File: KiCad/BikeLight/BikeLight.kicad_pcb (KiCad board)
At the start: 2 copper layers, 17 parts, among them J1 Conn-01x02_P2.5mm_S2B-XH-A-BK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, J3 Conn-01x02_P2.5mm_S2B-XH-A-BK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, SW1 CK_KMS2xxG, U1 HT-CT62, U2 MPU-6050, U3 MCP1826S-33, U4 MAX17048, U5 TP4056-42-ESOP8

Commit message: Added power protection, annotated
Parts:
- added C8: 100n_0603_TCC0603X7R104K500CT, Capacitor_SMD:C_0603_1608Metric, F.Cu at (166.6, 62.9)
- added J2: TYPE-C-31-M-12, Connector_USB:USB_C_Receptacle_G-Switch_GT-USB-7051x, F.Cu at (178.1, 65.3)
- added R10: 0R_0603_0603WAF0000T5E, Resistor_SMD:R_0603_1608Metric, F.Cu at (170.6, 67.9)
- added R11: 0R_0603_0603WAF0000T5E, Resistor_SMD:R_0603_1608Metric, F.Cu at (170.6, 70.4)
- added R12: 0R_0603_0603WAF0000T5E, Resistor_SMD:R_0603_1608Metric, F.Cu at (170.6, 72.9)
- added R3: 4.7k_0402_0402WGF4701TCE, Resistor_SMD:R_0603_1608Metric, F.Cu at (166.6, 65.4)
- added R4: 4.7k_0402_0402WGF4701TCE, Resistor_SMD:R_0603_1608Metric, F.Cu at (166.6, 67.9)
- added R5: 0R_0603_0603WAF0000T5E, Resistor_SMD:R_0603_1608Metric, F.Cu at (166.6, 70.4)
- added R6: 75k_0603_RC0603FR-0775KL, Resistor_SMD:R_0603_1608Metric, F.Cu at (166.6, 72.9)
- added R7: 0R_0603_0603WAF0000T5E, Resistor_SMD:R_0603_1608Metric, F.Cu at (166.6, 75.4)
- added R8: 0R_0603_0603WAF0000T5E, Resistor_SMD:R_0603_1608Metric, F.Cu at (170.6, 62.9)
- added R9: 0R_0603_0603WAF0000T5E, Resistor_SMD:R_0603_1608Metric, F.Cu at (170.6, 65.4)
- R1: value A1050 -> A1050 13
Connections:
- C6 pad 2: Net-(U1-GPIO8) -> Net-(C6-Pad2)
- R1 pad 1: unconnected-(R1-Pad1) -> +3.3V
- R1 pad 2: unconnected-(R1-Pad2) -> Net-(U1-GPIO2)
- SW1 pad 2: Net-(U1-GPIO8) -> Net-(C6-Pad2)
- U1 pad 14: unconnected-(U1-GPIO10-Pad14) -> /SCK
- U1 pad 15: unconnected-(U1-GPIO9-Pad15) -> Net-(U1-GPIO9)
- U1 pad 16: Net-(U1-GPIO8) -> /SX_NSS
- U1 pad 20: unconnected-(U1-GPIO21_TXD-Pad20) -> /IRQ_RFID
- U1 pad 3: unconnected-(U1-GPIO7-Pad3) -> /SX_MOSI
- U1 pad 4: unconnected-(U1-GPIO6-Pad4) -> /SX_MISO
- U1 pad 5: unconnected-(U1-GPIO5-Pad5) -> /SX_RST
- U1 pad 6: unconnected-(U1-GPIO4-Pad6) -> /SX_BUSY
- U1 pad 7: unconnected-(U1-GPIO3-Pad7) -> /SX_DIO1
- U1 pad 8: unconnected-(U1-GPIO2-Pad8) -> Net-(U1-GPIO2)
- U2 pad 3: /SCL -> unconnected-(U2-SCL-Pad3)
- U2 pad 4: /SDA -> unconnected-(U2-SDA-Pad4)
- U2 pad 5: unconnected-(U2-XDA-Pad5) -> Net-(U2-XDA)
- U2 pad 6: unconnected-(U2-XCL-Pad6) -> Net-(U2-XCL)
- U4 pad 7: /SCL -> Net-(U4-SCL)
- U4 pad 8: /SDA -> Net-(U4-SDA)

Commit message: Finished most of the PCB
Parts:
- added C1: 22u_0805_CL21A226MAQNNNE, Capacitor_SMD:C_0805_2012Metric, F.Cu at (100.0, 72.5)
- added C5: 1u_0603_CL10A105KA8NNNC, Capacitor_SMD:C_0603_1608Metric, F.Cu at (132.0, 89.3)
- added D1: SOD-882_0402_RCLAMP0521P-N, Diode_SMD:D_0402_1005Metric, F.Cu at (136.0, 84.5)
- added D2: 1N5819WS, Diode_SMD:D_SOD-323, F.Cu at (108.0, 76.0)
- added D3: 1N5819WS, Diode_SMD:D_SOD-323, F.Cu at (132.5, 84.5)
- added F1: MF-MSMF010-2, Fuse:Fuse_1812_4532Metric, F.Cu at (128.0, 83.5)
- added L1: 22u_620mA_1210_CBC3225T220KR, Inductor_SMD:L_1210_3225Metric, F.Cu at (104.0, 72.5)
- added Q1: AO3401A, Package_TO_SOT_SMD:SOT-23, F.Cu at (129.0, 89.5)
- added R1: 47k_0402_0402WGF1002TCE, Resistor_SMD:R_0603_1608Metric, F.Cu at (111.0, 73.0)
- added R17: 5.1k_0603_0603WAF5101T5E, Resistor_SMD:R_0603_1608Metric, F.Cu at (121.5, 68.5)
- added R18: 5.1k_0603_0603WAF5101T5E, Resistor_SMD:R_0603_1608Metric, F.Cu at (127.5, 74.5)
- added R19: 0R_0603_0603WAF0000T5E, Resistor_SMD:R_0603_1608Metric, F.Cu at (134.0, 71.5)
- added R2: 10k_0603_RC0603JR-0710KL, Resistor_SMD:R_0603_1608Metric, F.Cu at (111.0, 69.0)
- added R20: 0R_0603_0603WAF0000T5E, Resistor_SMD:R_0603_1608Metric, F.Cu at (137.5, 71.5)
- added R21: 0R_0603_0603WAF0000T5E, Resistor_SMD:R_0603_1608Metric, F.Cu at (166.5, 89.2)
- added R22: 0R_0603_0603WAF0000T5E, Resistor_SMD:R_0603_1608Metric, F.Cu at (166.5, 86.7)
- added R3: 10k_0603_RC0603JR-0710KL, Resistor_SMD:R_0603_1608Metric, F.Cu at (134.5, 84.5)
- added R6: 1k_0603_RMC06031K1%N, Resistor_SMD:R_0603_1608Metric, F.Cu at (129.5, 86.5)
- added U2: MT3608, Package_TO_SOT_SMD:SOT-23-6, F.Cu at (108.0, 71.0)
- added U6: RFID-RC522, Personal_Library:RFID_RC522, F.Cu at (191.5, 76.5)
- C4: value 100n_0603_TCC0603X7R104K500CT -> 22u_0805_CL21A226MAQNNNE; footprint Capacitor_SMD:C_0603_1608Metric -> Capacitor_SMD:C_0805_2012Metric
- J3: renamed from J2; value TYPE-C-31-M-12 -> GT-USB-7051A
- moved SW1 68.5 mm to (86.5, 102.0), turned to -90 degrees
- moved C6 66.2 mm to (90.8, 102.0), turned to -90 degrees
- moved R7 63.8 mm to (89.9, 99.5), turned to 180 degrees
- moved R4 51.2 mm to (122.0, 79.0), turned to 90 degrees
- moved J3 51.0 mm to (127.3, 70.2)
- moved R5 47.7 mm to (119.0, 79.0), turned to 90 degrees
- moved C7 38.1 mm to (135.2, 95.5)
- moved C8 36.6 mm to (148.0, 99.5)
- moved C4 36.4 mm to (113.0, 71.0), turned to 90 degrees
- moved C9 36.0 mm to (188.5, 91.5), turned to 90 degrees
- moved R8 34.3 mm to (151.0, 101.0), turned to 90 degrees
- moved U5 32.2 mm to (153.5, 88.5), turned to 0 degrees
- moved C2 32.0 mm to (120.0, 86.5)
- moved J1 31.8 mm to (94.8, 72.0), turned to -90 degrees
- moved R14 23.3 mm to (187.5, 84.0)
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- renumbered C5 to C10, C7 to C2, C1 to C3, C2 to C7, C3 to C8, C8 to C9, J3 to J1, J1 to J2, R4 to R10, R1 to R11, R6 to R12, R9 to R13, R10 to R14, R11 to R15, R12 to R16, R8 to R4, R7 to R5, R2 to R7, R5 to R8, R3 to R9, U5 to U1, U4 to U3, U3 to U4, U1 to U5, U2 to U7
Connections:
- net Net-(J2-VBUS-PadA4) renamed VBUS
- C4 pad 1: GND -> VSOL
- J1 pad 1: Net-(J3-Pin_1) -> +SOLAR
- J1 pad 2: Net-(J3-Pin_2) -> GND
- J3 pad A1: Net-(J2-GND-PadA1) -> GND
- J3 pad A12: Net-(J2-GND-PadA1) -> GND
- J3 pad A5: unconnected-(J2-CC1-PadA5) -> Net-(J3-CC1)
- J3 pad A6: unconnected-(J2-D+-PadA6) -> Net-(J3-D+-PadA6)
- J3 pad A7: unconnected-(J2-D--PadA7) -> Net-(J3-D--PadA7)
- J3 pad B1: Net-(J2-GND-PadA1) -> GND
- J3 pad B12: Net-(J2-GND-PadA1) -> GND
- J3 pad B5: unconnected-(J2-CC2-PadB5) -> Net-(J3-CC2)
- J3 pad B6: unconnected-(J2-D+-PadB6) -> Net-(J3-D+-PadA6)
- J3 pad B7: unconnected-(J2-D--PadB7) -> Net-(J3-D--PadA7)
- J3 pad S1: unconnected-(J2-SHIELD-PadS1) -> GND
- R5 pad 1: /SDA -> Net-(U3-SDA)
- R5 pad 2: Net-(U4-SDA) -> /SDA
- U1 pad 1: Net-(J3-Pin_1) -> VSOL
- U1 pad 2: Net-(J3-Pin_2) -> GND
- U3 pad 8: Net-(U4-SDA) -> Net-(U3-SDA)
- U4 pad 1: +BATT -> Net-(D3-K)
- U5 pad 17: unconnected-(U1-GPIO18_DN-Pad17) -> /USB_DN
- U5 pad 18: unconnected-(U1-GPIO19_DP-Pad18) -> /USB_DP
- U5 pad 19: unconnected-(U1-GPIO20_RXD-Pad19) -> /ACC_INT
- U7 pad 3: unconnected-(U2-SCL-Pad3) -> Net-(U7-SCL)
- U7 pad 4: unconnected-(U2-SDA-Pad4) -> Net-(U7-SDA)
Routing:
- net /SDA: track 0.00 -> 103.3 mm, vias 0 -> 3
- net /SCL: track 0.00 -> 102.9 mm, vias 0 -> 3
- net Net-(C6-Pad2): track 0.00 -> 70.3 mm
- net GND: track 2.49 -> 57.5 mm, vias 0 -> 17
- net /IRQ_RFID: track 0.00 -> 47.7 mm
- net /USB_DP: track 0.00 -> 33.5 mm
- net /USB_DN: track 0.00 -> 33.2 mm
- net VSOL: track 0.00 -> 32.8 mm
- net VBUS: track 0.00 -> 26.5 mm, vias 0 -> 3
- net Net-(J3-Pin_1): track 24.4 -> 0.00 mm
- net Net-(J3-D--PadA7): track 0.00 -> 23.6 mm
- net +BATT: track 29.0 -> 48.6 mm
- net Net-(J3-D+-PadA6): track 0.00 -> 16.8 mm
- net Net-(J3-Pin_2): track 16.4 -> 0.00 mm
- net +SOLAR: track 0.00 -> 15.7 mm
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- added copper zone on F.Cu, net +3.3V
- added copper zone on B.Cu, net GND
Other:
- board outline added: 170.5 x 50 mm

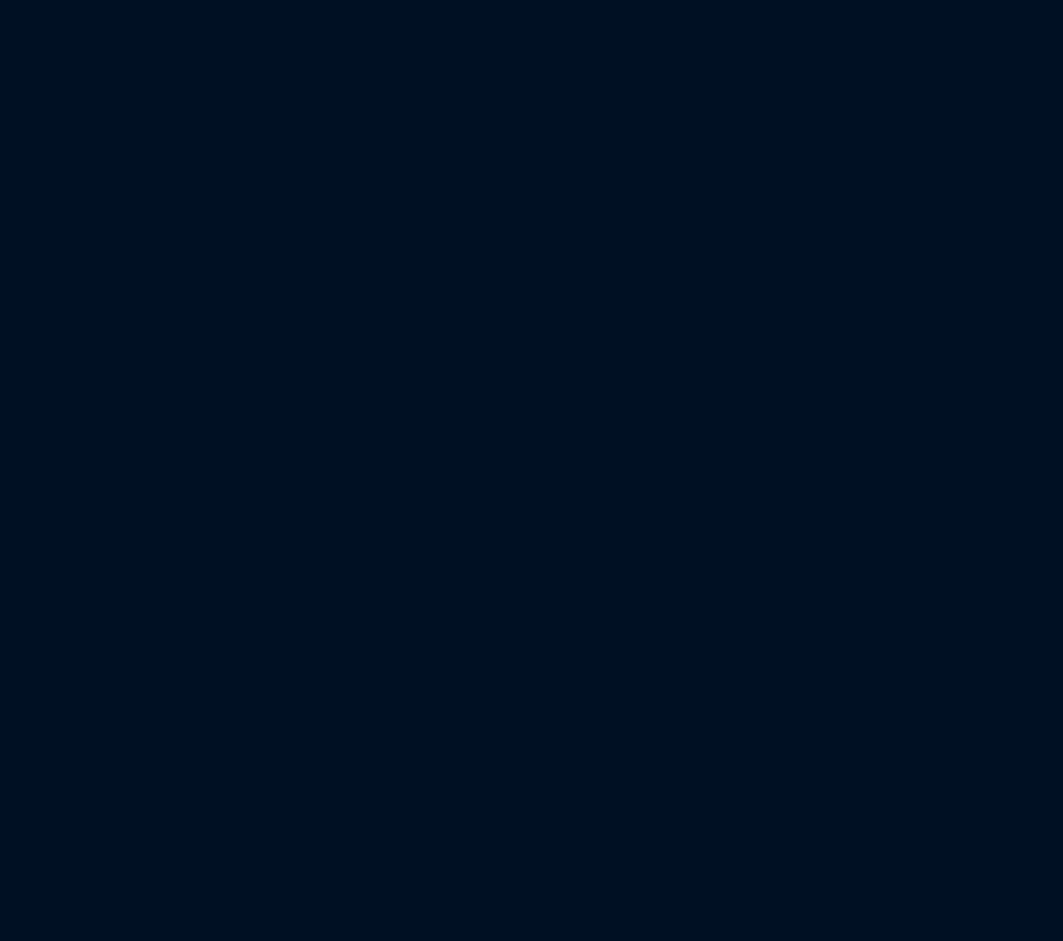
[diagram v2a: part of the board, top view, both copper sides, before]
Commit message: Added Busser and LED controller
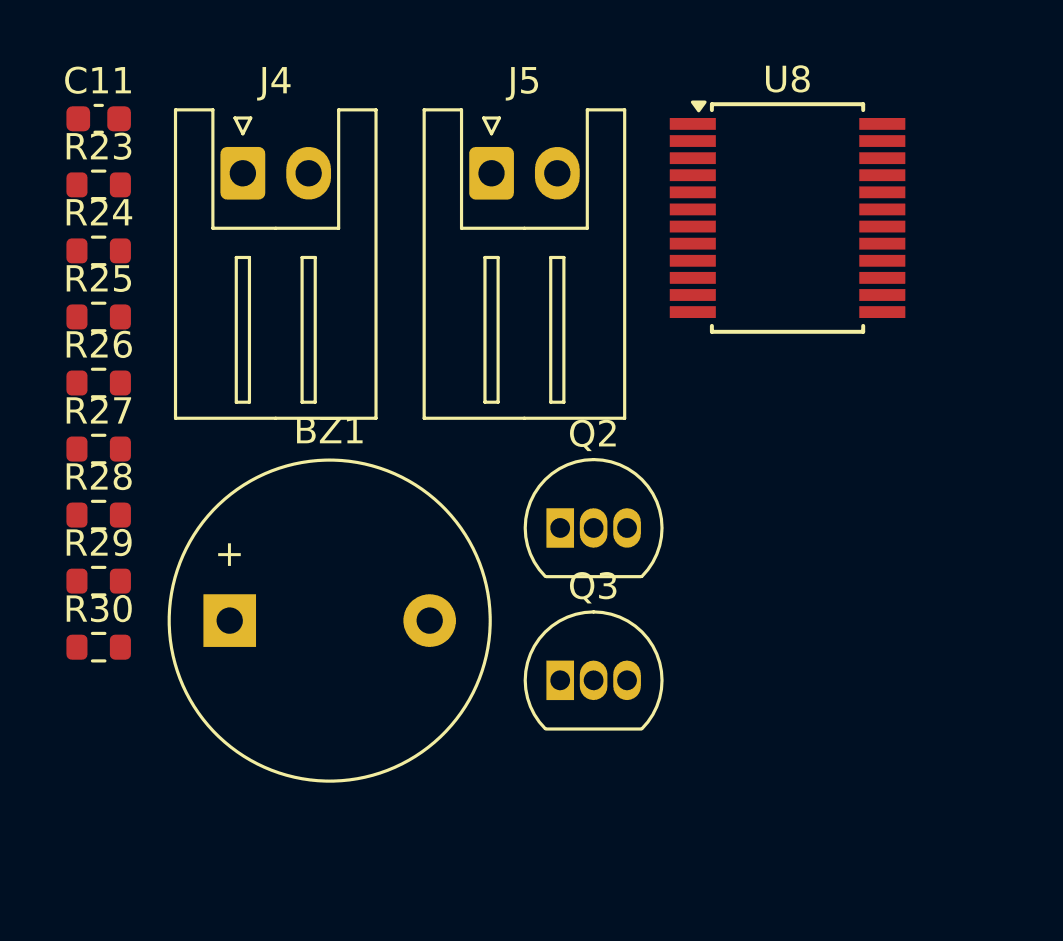
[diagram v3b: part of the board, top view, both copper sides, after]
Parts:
- added BZ1: TMB12A03, Buzzer_Beeper:Buzzer_12x9.5RM7.6, F.Cu at (6.49, 19.8)
- added C11: 100n_0603_TCC0603X7R104K500CT, Capacitor_SMD:C_0603_1608Metric, F.Cu at (1.50, 0.76)
- added J4: Conn-01x02_P2.5mm_S2B-XH-A-BK(LF)(SN), Connector_JST:JST_XH_S2B-XH-A_1x02_P2.50mm_Horizontal, F.Cu at (6.99, 2.83)
- added J5: Conn-01x02_P2.5mm_S2B-XH-A-BK(LF)(SN), Connector_JST:JST_XH_S2B-XH-A_1x02_P2.50mm_Horizontal, F.Cu at (16.4, 2.83)
- added Q2: BC337, Package_TO_SOT_THT:TO-92_Inline, F.Cu at (19.0, 16.3)
- added Q3: BC337, Package_TO_SOT_THT:TO-92_Inline, F.Cu at (19.0, 22.1)
- added R23: 0R_0603_0603WAF0000T5E, Resistor_SMD:R_0603_1608Metric, F.Cu at (1.50, 3.27)
- added R24: 0R_0603_0603WAF0000T5E, Resistor_SMD:R_0603_1608Metric, F.Cu at (1.50, 5.78)
- added R25: 0R_0603_0603WAF0000T5E, Resistor_SMD:R_0603_1608Metric, F.Cu at (1.50, 8.29)
- added R26: 0R_0603_0603WAF0000T5E, Resistor_SMD:R_0603_1608Metric, F.Cu at (1.50, 10.8)
- added R27: 0R_0603_0603WAF0000T5E, Resistor_SMD:R_0603_1608Metric, F.Cu at (1.50, 13.3)
- added R28: 0R_0603_0603WAF0000T5E, Resistor_SMD:R_0603_1608Metric, F.Cu at (1.50, 15.8)
- added R29: 1k_0603_RMC06031K1%N, Resistor_SMD:R_0603_1608Metric, F.Cu at (1.50, 18.3)
- added R30: 1k_0603_RMC06031K1%N, Resistor_SMD:R_0603_1608Metric, F.Cu at (1.50, 20.8)
- added U8: PCA9555DB, Package_SO:SSOP-24_5.3x8.2mm_P0.65mm, F.Cu at (27.7, 4.53)
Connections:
- R13 pad 1: /SDA -> /RF_NSS
- R14 pad 1: /SCL -> /SX_MISO
- U5 pad 19: /ACC_INT -> /RF_NSS
- U5 pad 20: /IRQ_RFID -> /IRQ
- U6 pad 2: unconnected-(U6-SCK/ADR_1-Pad2) -> Net-(U6-SCK/ADR_1)
- U6 pad 3: unconnected-(U6-MOSI/ADR_0-Pad3) -> Net-(U6-MOSI/ADR_0)
- U6 pad 5: /IRQ_RFID -> Net-(U6-IRQ)
- U7 pad 8: /ACC_INT -> Net-(U7-INT)
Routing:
- net (no net): track 0.00 -> 62.9 mm
- net /IRQ_RFID: track 47.7 -> 0.00 mm
- net /ACC_INT: track 15.1 -> 0.00 mm

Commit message: Comenting files
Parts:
- removed the R19 at (134.0, 71.5)
- removed the R20 at (137.5, 71.5)
- added Q2: AO3400A, Package_TO_SOT_SMD:SOT-23, F.Cu at (137.2, 132.2)
- moved J4 247.4 mm to (237.4, 92.8), turned to 90 degrees
- moved J5 234.9 mm to (237.6, 82.2), turned to 90 degrees
- moved R14 201.8 mm to (187.5, 86.7)
- moved R11 200.9 mm to (187.5, 79.1)
- moved R12 200.9 mm to (187.5, 81.6)
- moved R5 186.2 mm to (164.9, 100.0)
- moved BZ1 172.3 mm to (171.0, 70.9)
- moved Q3 161.6 mm to (144.7, 118.0)
- moved Q4 161.6 mm to (144.7, 123.8)
- moved R27 161.6 mm to (127.1, 120.0)
- moved R28 161.6 mm to (127.1, 122.5)
- moved U7 145.3 mm to (134.5, 103.0), turned to 90 degrees
- moved C10 102.8 mm to (67.4, 79.6)
- moved R20 102.8 mm to (67.4, 94.7)
- moved R19 102.8 mm to (67.4, 92.2)
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- renumbered C10 to C1, C11 to C10, C8 to C11, C3 to C2, C2 to C3, C5 to C4, C7 to C5, C9 to C6, C1 to C7, C4 to C8, C6 to C9, D3 to D2, D2 to D3, J2 to J1, J1 to J2, Q2 to Q3, Q3 to Q4, R22 to R1, R13 to R10, R23 to R11, R24 to R12, R14 to R13, R25 to R14, R1 to R15, R2 to R16, R7 to R17, R8 to R18, R27 to R19, R21 to R2, R28 to R20, R9 to R21, R17 to R22, R18 to R23, R10 to R24, R11 to R25, R12 to R26, R29 to R27, R30 to R28, R15 to R3, R16 to R4, R26 to R5, R3 to R6, R6 to R7, R4 to R8, R5 to R9, U7 to U2, U6 to U5, U2 to U6, U8 to U7, U5 to U8
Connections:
- BZ1 pad 1: unconnected-(BZ1-+-Pad1) -> Net-(BZ1-+)
- BZ1 pad 2: unconnected-(BZ1---Pad2) -> GND
- J3 pad A6: Net-(J3-D+-PadA6) -> /USB_DP
- J3 pad A7: Net-(J3-D--PadA7) -> /USB_DN
- J3 pad B6: Net-(J3-D+-PadA6) -> /USB_DP
- J3 pad B7: Net-(J3-D--PadA7) -> /USB_DN
- R27 pad 2: Net-(R29-Pad2) -> /LED
- R28 pad 1: Net-(R29-Pad2) -> /LED
- U1 pad 3: unconnected-(U1-OUT--Pad3) -> GND
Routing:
- net (no net): track 62.9 -> 0.00 mm
- net /SX_MISO: track 0.00 -> 49.9 mm
- net /SCK: track 0.00 -> 49.7 mm, vias 0 -> 2
- net /SX_MOSI: track 0.00 -> 49.3 mm, vias 0 -> 2
- net /RF_NSS: track 0.00 -> 45.2 mm
- net /IRQ: track 0.00 -> 36.3 mm
- net /SCL: track 102.9 -> 70.5 mm
- net /SDA: track 103.3 -> 71.2 mm
- net /USB_DP: track 33.5 -> 63.3 mm
- net /USB_DN: track 33.2 -> 62.7 mm, vias 0 -> 2
- net Net-(J3-D--PadA7): track 23.6 -> 0.00 mm
- net Net-(J3-D+-PadA6): track 16.8 -> 0.00 mm
- net VBUS: track 26.5 -> 19.8 mm
- net Net-(U2-INT): track 0.00 -> 4.57 mm
- net Net-(J3-CC2): track 3.57 -> 6.99 mm, vias 0 -> 2
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
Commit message: Gerber generation
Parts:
- removed C10: 100n_0603_TCC0603X7R104K500CT, Capacitor_SMD:C_0603_1608Metric
- removed D1: SOD-882_0402_RCLAMP0521P-N, Diode_SMD:D_0402_1005Metric
- removed Q4: BC337, Package_TO_SOT_THT:TO-92_Inline
- removed R20: 0R_0603_0603WAF0000T5E, Resistor_SMD:R_0603_1608Metric
- removed SW1: CK_KMS2xxG, Button_Switch_SMD:SW_SPST_CK_KMS2xxGP
- removed U7: PCA9555DB, Package_SO:SSOP-24_5.3x8.2mm_P0.65mm
- added C12: 100n_0603_TCC0603X7R104K500CT, Capacitor_SMD:C_0603_1608Metric, F.Cu at (126.1, 99.4)
- added D4: SMAJ5.0CA/TR13_NONAME, Diode_SMD:D_SMA, F.Cu at (137.8, 83.4)
- added J6: Conn_01x05, Connector_PinHeader_2.54mm:PinHeader_1x05_P2.54mm_Horizontal, F.Cu at (219.1, 74.4)
- added R28: 100R_0603_RC0603FR-07100RL, Resistor_SMD:R_0603_1608Metric, F.Cu at (126.1, 95.9)
- added R31: 100k_0603_RC0603FR-07100KL, Resistor_SMD:R_0603_1608Metric, F.Cu at (143.6, 102.8)
- added SW2: SW_PB_B3F-4055, 00-kiml-switch-button-tht:SW_PB_B3F-4055, F.Cu at (134.7, 102.9)
- added SW3: K2-1102AQ-H4CW-01, Personal_Library:SW_Tactile_SPST_Angled_K2-1102AQ-H4CW-01, F.Cu at (88.1, 105.3)
- Q3: value BC337 -> BC847BDW1; footprint Package_TO_SOT_THT:TO-92_Inline -> Package_TO_SOT_SMD:SOT-363_SC-70-6
- R19: value 0R_0603_0603WAF0000T5E -> 100k_0603_RC0603FR-07100KL
- moved R30 99.0 mm to (216.8, 80.6)
- moved R29 96.8 mm to (216.8, 83.6), turned to 180 degrees
- moved Q3 86.1 mm to (222.9, 82.0)
- moved R19 86.1 mm to (153.0, 101.0), turned to 90 degrees
- moved Q2 68.2 mm to (164.6, 69.7), turned to 90 degrees
- moved R17 6.28 mm to (96.2, 99.4), turned to 0 degrees
- moved C9 4.65 mm to (95.4, 102.0)
- moved R1 0.30 mm to (166.2, 86.7)
- moved R2 0.30 mm to (166.2, 89.2)
- moved R3 0.30 mm to (166.2, 91.7)
- moved R4 0.30 mm to (166.2, 94.2)
- moved J5 0.09 mm to (237.5, 82.2)
- renumbered R21 to R22, R22 to R23, R23 to R24, R24 to R25, R25 to R26, R26 to R27, R27 to R29, R28 to R30
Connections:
- C2 pad 1: +BATT -> VOUT
- Q1 pad 3: +BATT -> VOUT
- Q2 pad 1: /BUSSER -> /BUZZER
- Q3 pad 1: +3.3V -> Net-(J5-Pin_1)
- Q3 pad 2: Net-(Q3-B) -> Net-(Q3A-B1)
- Q3 pad 3: Net-(J4-Pin_1) -> +3.3V
- R10 pad 1: /RF_NSS -> /IRQ
- R18 pad 2: Net-(U8-GPIO9) -> /IRQ
- R19 pad 1: /SCL -> +3.3V
- R19 pad 2: Net-(U7-SCL) -> /IRQ
- R26 pad 2: Net-(U8-GPIO2) -> /BUZZER
- R27 pad 1: Net-(U8-GPIO2) -> /BUZZER
- R29 pad 1: Net-(Q3-B) -> Net-(Q3B-B2)
- R30 pad 2: Net-(Q4-B) -> Net-(Q3A-B1)
- U1 pad 6: unconnected-(U1-OUT+-Pad6) -> VOUT
- U8 pad 11: unconnected-(U8-EN-Pad11) -> Net-(U8-EN)
- U8 pad 15: Net-(U8-GPIO9) -> /LED
- U8 pad 19: /RF_NSS -> /GNSS_RX
- U8 pad 8: Net-(U8-GPIO2) -> /BUZZER
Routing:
- net /GNSS_RX: track 0.00 -> 83.4 mm, vias 0 -> 2
- net /LED: track 0.00 -> 80.7 mm, vias 0 -> 2
- net Net-(U8-EN): track 0.00 -> 58.4 mm, vias 0 -> 1
- net /RF_NSS: track 45.2 -> 0.00 mm
- net VOUT: track 0.00 -> 34.1 mm
- net +BATT: track 48.6 -> 17.4 mm
- net /BUZZER: track 0.00 -> 25.2 mm
- net Net-(J4-Pin_1): track 0.00 -> 21.3 mm
- net /IRQ: track 36.3 -> 55.6 mm, vias 0 -> 2
- net Net-(J5-Pin_1): track 0.00 -> 16.7 mm
- net Net-(U8-GPIO2): track 11.7 -> 0.00 mm
- net VBUS: track 19.8 -> 31.1 mm
- net Net-(Q3B-B2): track 0.00 -> 7.39 mm
- net Net-(C9-Pad2): track 70.3 -> 64.2 mm
- net Net-(BZ1-+): track 0.00 -> 5.56 mm
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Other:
- rule pad_to_mask_clearance: 0 -> 0.038
- board text added: "Back Light"
- board text added: "Battery"
- board text added: "BikeLight Group 1"
- board text added: "Front Light"
- board text added: "Solar Connector"
